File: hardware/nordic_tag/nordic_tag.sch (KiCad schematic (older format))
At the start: 6 parts

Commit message: Started PCB + BOM
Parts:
- AE101: renamed from AE?; footprint (none) -> nordic_tag:RFANT3216120A5T
- C101: renamed from C?; footprint (none) -> Capacitor_SMD:C_0603_1608Metric
- J101: renamed from J?; footprint (none) -> Connector_USB:USB_Micro-B_Wuerth_629105150521
- J102: renamed from J?; footprint (none) -> Connector_PinHeader_2.54mm:PinHeader_1x08_P2.54mm_Vertical
- L101: renamed from L?; footprint (none) -> Inductor_SMD:L_0603_1608Metric
- gave numbers to parts that had none: 1
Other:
- moved on the sheet: AE101, C101, J101, J102, L101, U101

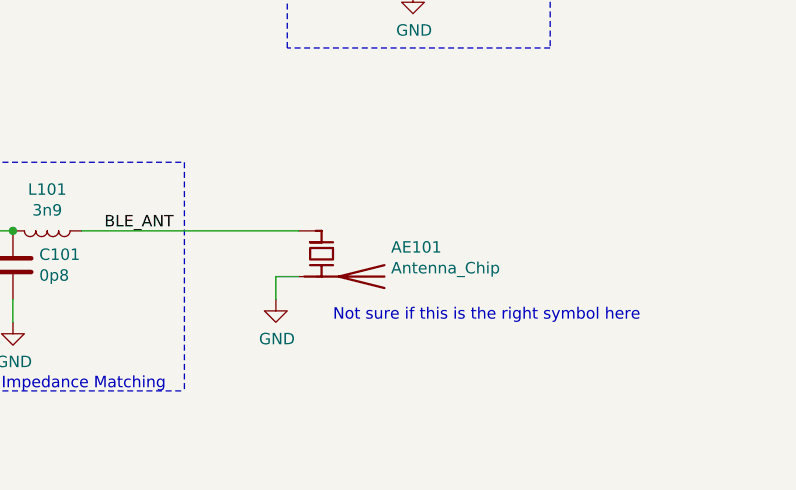
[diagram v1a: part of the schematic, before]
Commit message: Switched to pcb antenna. started placement
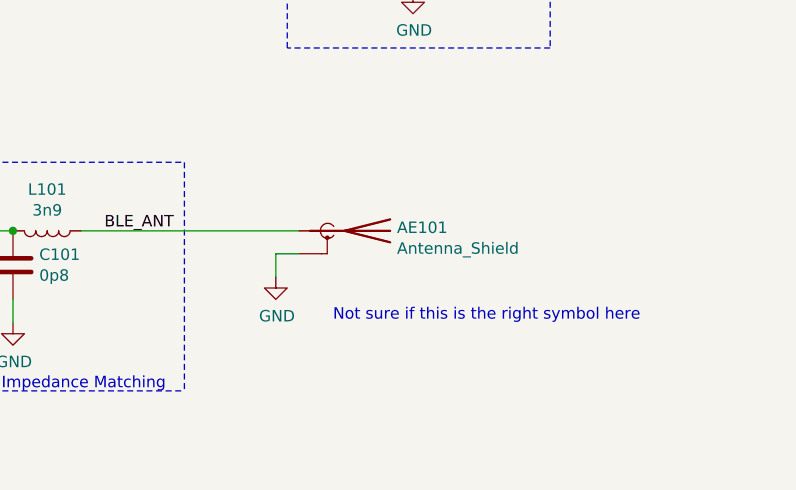
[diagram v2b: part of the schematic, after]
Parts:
- removed AE101: Antenna_Chip, nordic_tag:RFANT3216120A5T, symbol Device:Antenna_Chip
- added AE101: Antenna_Shield, RF_Antenna:Texas_SWRA117D_2.4GHz_Right, symbol Device:Antenna_Shield
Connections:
- net BLE_ANT: now also AE101.1 (A)
- net GND: now also AE101.2 (Shield)
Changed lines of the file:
@@
 Wire Wire Line
 	7000 4450 7950 4450
-$Comp
-L Device:Antenna_Chip AE101
-U 1 1 5DD9ADD7
-P 8050 4550
-F 0 "AE101" V 8022 4854 50  0000 L CNN
-F 1 "Antenna_Chip" V 8113 4854 50  0000 L CNN
-F 2 "nordic_tag:RFANT3216120A5T" H 7950 4725 50  0001 C CNN
-F 3 "~" H 7950 4725 50  0001 C CNN
-	1    8050 4550
-	0    1    1    0
-$EndComp
 Wire Wire Line
-	7950 4650 7850 4650
+	7950 4550 7850 4550
 Wire Wire Line
-	7850 4650 7850 4750
+	7850 4550 7850 4650
 $Comp
 L power:GND #PWR0104
 U 1 1 5DD9C25C
-P 7850 4750
-F 0 "#PWR0104" H 7850 4500 50  0001 C CNN
-F 1 "GND" H 7855 4577 50  0000 C CNN
-F 2 "" H 7850 4750 50  0001 C CNN
-F 3 "" H 7850 4750 50  0001 C CNN
-	1    7850 4750
+P 7850 4650
+F 0 "#PWR0104" H 7850 4400 50  0001 C CNN
+F 1 "GND" H 7855 4477 50  0000 C CNN
+F 2 "" H 7850 4650 50  0001 C CNN
+F 3 "" H 7850 4650 50  0001 C CNN
+	1    7850 4650
 	1    0    0    -1
 $EndComp
 Text Notes 8100 4850 0    50   ~ 0
 Not sure if this is the right symbol here
+$Comp
+L Device:Antenna_Shield AE101
+U 1 1 5DCA5F54
+P 8150 4450
+F 0 "AE101" V 8136 4680 50  0000 L CNN
+F 1 "Antenna_Shield" V 8227 4680 50  0000 L CNN
+F 2 "RF_Antenna:Texas_SWRA117D_2.4GHz_Right" H 8150 4550 50  0001 C CNN
+F 3 "~" H 8150 4550 50  0001 C CNN
+	1    8150 4450
+	0    1    1    0
+$EndComp
 $EndSCHEMATC
